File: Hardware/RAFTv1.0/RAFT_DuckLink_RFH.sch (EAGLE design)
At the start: 127 parts, among them J1 AMPHENOL_132134, J2 AMPHENOL_132134, J4 Micro-USB, J5 132134-15, Q1 SIA817EDJ, Q2 SI7288DP, Q3 2N7002, U1 SX1276, U10 PE4259, U2 MAX2771ETI+, U3 ESP32-D0WD, U4 W25Q16BVSSIG, U5 INTERFACE-CP2102-GMR(QFN28), U6 PE4259, U7 SP0503BAHT, U8 BQ24650RVAR, U9 TPS63070RNMT, Y1 32.768kHz

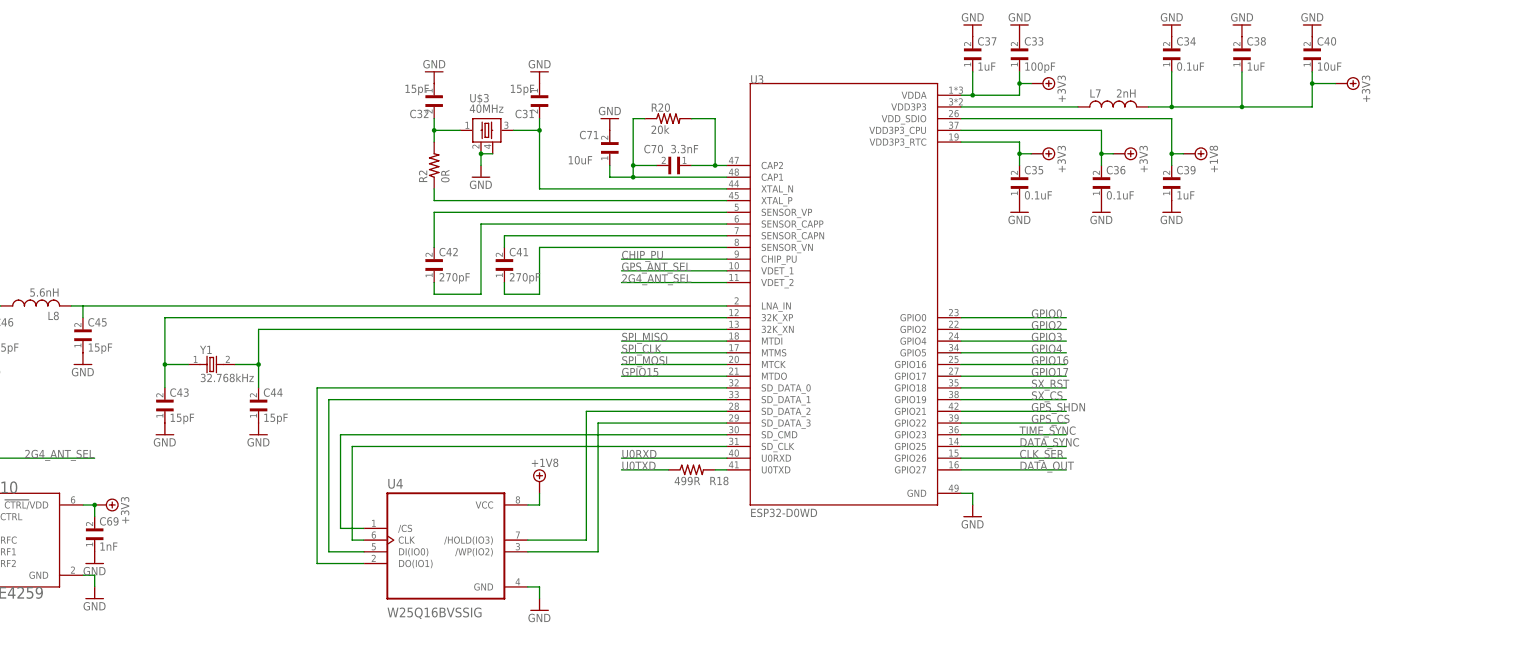
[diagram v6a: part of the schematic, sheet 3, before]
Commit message: fixed uart, updated pins
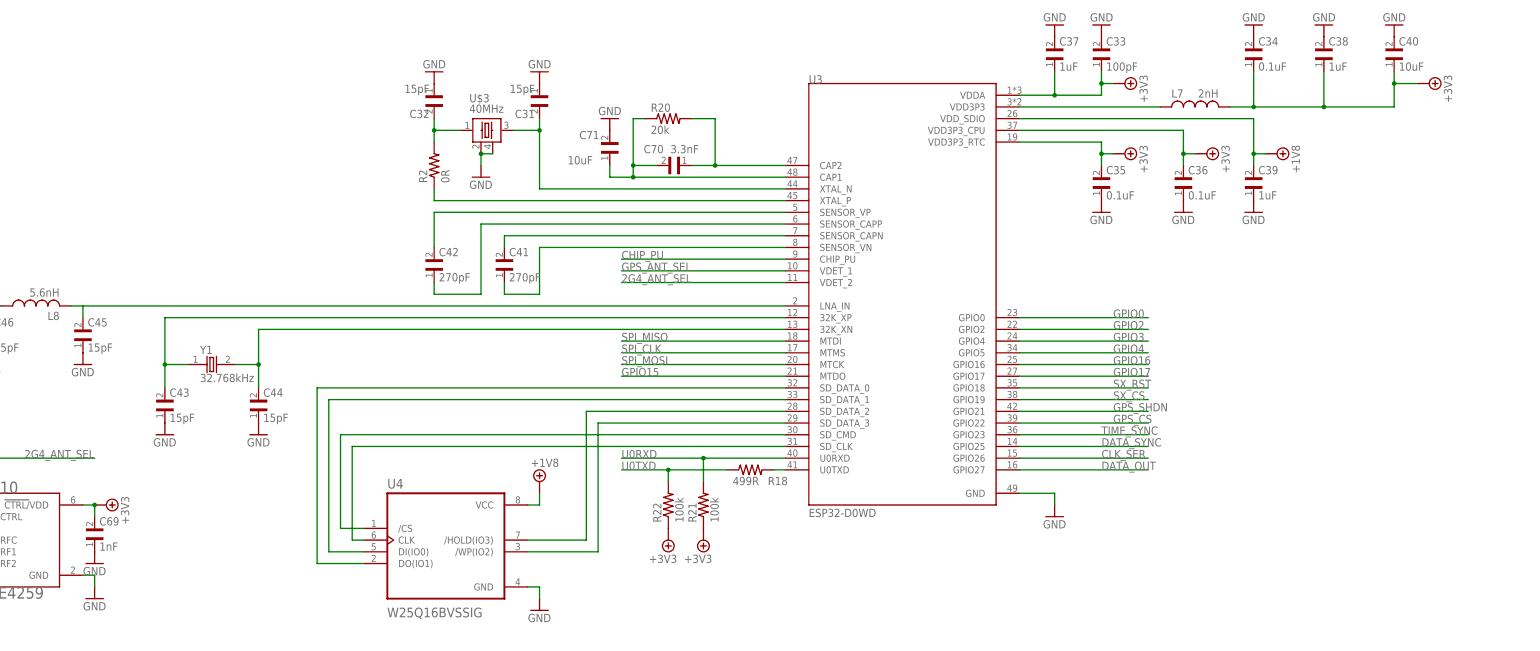
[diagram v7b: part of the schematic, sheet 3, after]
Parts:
- added R21, R22: 100k, RAFT-components:CRCW0402100KFKED
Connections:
- net +3.3V: now also R21.1, R22.1
- net U0RXD: now also R21.2
- net U0TXD: now also R22.2
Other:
- moved on the sheet: C33, C34, C35, C36, C37, C38, C39, C40, L7, R18, U3

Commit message: added libs for headers and switches (SparkFun). added sch page for io headers
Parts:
- added J3: (no value), SparkFun-Connectors:CONN_10X2
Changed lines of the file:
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@@
 <layer number="48" name="Document" color="7" fill="1" visible="no" active="no"/>
 <layer number="49" name="Reference" color="7" fill="1" visible="no" active="no"/>
+<layer number="50" name="dxf" color="7" fill="1" visible="no" active="no"/>
 <layer number="51" name="tDocu" color="7" fill="1" visible="no" active="no"/>
 <layer number="52" name="bDocu" color="7" fill="1" visible="no" active="no"/>
+<layer number="53" name="tGND_GNDA" color="7" fill="9" visible="no" active="no"/>
+<layer number="54" name="bGND_GNDA" color="1" fill="9" visible="no" active="no"/>
+<layer number="56" name="wert" color="7" fill="1" visible="no" active="no"/>
+<layer number="57" name="tCAD" color="7" fill="1" visible="no" active="no"/>
+<layer number="59" name="tCarbon" color="7" fill="1" visible="no" active="no"/>
+<layer number="60" name="bCarbon" color="7" fill="1" visible="no" active="no"/>
 <layer number="88" name="SimResults" color="9" fill="1" visible="yes" active="yes"/>
 <layer number="89" name="SimProbes" color="9" fill="1" visible="yes" active="yes"/>
@@
 <layer number="98" name="Guide" color="6" fill="1" visible="yes" active="yes"/>
 <layer number="99" name="SpiceOrder" color="7" fill="1" visible="yes" active="yes"/>
+<layer number="100" name="Muster" color="7" fill="1" visible="no" active="no"/>
+<layer number="101" name="Patch_Top" color="12" fill="4" visible="no" active="no"/>
+<layer number="102" name="Vscore" color="7" fill="1" visible="no" active="no"/>
+<layer number="103" name="tMap" color="7" fill="1" visible="no" active="no"/>
+<layer number="104" name="Name" color="16" fill="1" visible="no" active="no"/>
+<layer number="105" name="tPlate" color="7" fill="1" visible="no" active="no"/>
+<layer number="106" name="bPlate" color="7" fill="1" visible="no" active="no"/>
+<layer number="107" name="Crop" color="7" fill="1" visible="no" active="no"/>
+<layer number="108" name="tplace-old" color="10" fill="1" visible="no" active="no"/>
+<layer number="109" name="ref-old" color="11" fill="1" visible="no" active="no"/>
+<layer number="110" name="fp0" color="7" fill="1" visible="no" active="no"/>
+<layer number="111" name="LPC17xx" color="7" fill="1" visible="no" active="no"/>
+<layer number="112" name="tSilk" color="7" fill="1" visible="no" active="no"/>
+<layer number="113" name="IDFDebug" color="4" fill="1" visible="no" active="no"/>
+<layer number="114" name="Badge_Outline" color="7" fill="1" visible="no" active="no"/>
+<layer number="115" name="ReferenceISLANDS" color="7" fill="1" visible="no" active="no"/>
+<layer number="116" name="Patch_BOT" color="9" fill="4" visible="no" active="no"/>
+<layer number="117" name="PM_Ref" color="7" fill="1" visible="no" active="no"/>
+<layer number="118" name="Rect_Pads" color="7" fill="1" visible="no" active="no"/>
+<layer number="119" name="PF_Ref" color="7" fill="1" visible="no" active="no"/>
+<layer number="120" name="WFL_Ref" color="7" fill="1" visible="no" active="no"/>
+<layer number="121" name="_tsilk" color="7" fill="1" visible="no" active="no"/>
+<layer number="122" name="_bsilk" color="7" fill="1" visible="no" active="no"/>
+<layer number="123" name="tTestmark" color="7" fill="1" visible="no" active="no"/>
+<layer number="124" name="bTestmark" color="7" fill="1" visible="no" active="no"/>
+<layer number="125" name="_tNames" color="7" fill="1" visible="no" active="no"/>
+<layer number="126" name="_bNames" color="7" fill="1" visible="no" active="no"/>
+<layer number="127" name="_tValues" color="7" fill="1" visible="no" active="no"/>
+<layer number="128" name="_bValues" color="7" fill="1" visible="no" active="no"/>
+<layer number="129" name="Mask" color="7" fill="1" visible="no" active="no"/>
+<layer number="131" name="tAdjust" color="7" fill="1" visible="no" active="no"/>
+<layer number="132" name="bAdjust" color="7" fill="1" visible="no" active="no"/>
+<layer number="144" name="Drill_legend" color="7" fill="1" visible="no" active="no"/>
+<layer number="150" name="Notes" color="7" fill="1" visible="no" active="no"/>
+<layer number="151" name="HeatSink" color="7" fill="1" visible="no" active="no"/>
+<layer number="152" name="_bDocu" color="7" fill="1" visible="no" active="no"/>
+<layer number="153" name="FabDoc1" color="7" fill="1" visible="no" active="no"/>
+<layer number="154" name="FabDoc2" color="7" fill="1" visible="no" active="no"/>
+<layer number="155" name="FabDoc3" color="7" fill="1" visible="no" active="no"/>
+<layer number="199" name="Contour" color="7" fill="1" visible="no" active="no"/>
+<layer number="200" name="200bmp" color="1" fill="10" visible="no" active="no"/>
+<layer number="201" name="201bmp" color="2" fill="10" visible="no" active="no"/>
+<layer number="202" name="202bmp" color="3" fill="10" visible="no" active="no"/>
+<layer number="203" name="203bmp" color="4" fill="10" visible="no" active="no"/>
+<layer number="204" name="204bmp" color="5" fill="10" visible="no" active="no"/>
+<layer number="205" name="205bmp" color="6" fill="10" visible="no" active="no"/>
+<layer number="206" name="206bmp" color="7" fill="10" visible="no" active="no"/>
+<layer number="207" name="207bmp" color="8" fill="10" visible="no" active="no"/>
+<layer number="208" name="208bmp" color="9" fill="10" visible="no" active="no"/>
+<layer number="209" name="209bmp" color="7" fill="1" visible="no" active="no"/>
+<layer number="210" name="210bmp" color="7" fill="1" visible="no" active="no"/>
+<layer number="211" name="211bmp" color="7" fill="1" visible="no" active="no"/>
+<layer number="212" name="212bmp" color="7" fill="1" visible="no" active="no"/>
+<layer number="213" name="213bmp" color="7" fill="1" visible="no" active="no"/>
+<layer number="214" name="214bmp" color="7" fill="1" visible="no" active="no"/>
+<layer number="215" name="215bmp" color="7" fill="1" visible="no" active="no"/>
+<layer number="216" name="216bmp" color="7" fill="1" visible="no" active="no"/>
+<layer number="217" name="217bmp" color="18" fill="1" visible="no" active="no"/>
+<layer number="218" name="218bmp" color="19" fill="1" visible="no" active="no"/>
+<layer number="219" name="219bmp" color="20" fill="1" visible="no" active="no"/>
+<layer number="220" name="220bmp" color="21" fill="1" visible="no" active="no"/>
+<layer number="221" name="221bmp" color="22" fill="1" visible="no" active="no"/>
+<layer number="222" name="222bmp" color="23" fill="1" visible="no" active="no"/>
+<layer number="223" name="223bmp" color="24" fill="1" visible="no" active="no"/>
+<layer number="224" name="224bmp" color="25" fill="1" visible="no" active="no"/>
+<layer number="225" name="225bmp" color="7" fill="1" visible="no" active="no"/>
+<layer number="226" name="226bmp" color="7" fill="1" visible="no" active="no"/>
+<layer number="227" name="227bmp" color="7" fill="1" visible="no" active="no"/>
+<layer number="228" name="228bmp" color="7" fill="1" visible="no" active="no"/>
+<layer number="229" name="229bmp" color="7" fill="1" visible="no" active="no"/>
+<layer number="230" name="230bmp" color="7" fill="1" visible="no" active="no"/>
+<layer number="231" name="231bmp" color="7" fill="1" visible="no" active="no"/>
+<layer number="232" name="Eagle3D_PG2" color="7" fill="1" visible="no" active="no"/>
+<layer number="233" name="Eagle3D_PG3" color="7" fill="1" visible="no" active="no"/>
+<layer number="248" name="Housing" color="7" fill="1" visible="no" active="no"/>
+<layer number="249" name="Edge" color="7" fill="1" visible="no" active="no"/>
+<layer number="250" name="Descript" color="3" fill="1" visible="no" active="no"/>
+<layer number="251" name="SMDround" color="12" fill="11" visible="no" active="no"/>
+<layer number="254" name="cooling" color="7" fill="1" visible="no" active="no"/>
+<layer number="255" name="routoute" color="7" fill="1" visible="no" active="no"/>
 </layers>
 <schematic xreflabel="%F%N/%S.%C%R" xrefpart="/%S.%C%R">
@@
 <part name="SUPPLY19" library="supply3" deviceset="+3V3" device=""/>
 <part name="SUPPLY20" library="supply3" deviceset="+3V3" device=""/>
+<part name="J3" library="SparkFun-Connectors" deviceset="CONN_10X2" device=""/>
 </parts>
 <sheets>
@@
 </nets>
 </sheet>
+<sheet>
+<plain>
+</plain>
+<instances>
+<instance part="J3" gate="G$1" x="2.54" y="20.32" smashed="yes">
+<attribute name="VALUE" x="-1.27" y="2.794" size="1.778" layer="96" font="vector"/>
+<attribute name="NAME" x="-1.27" y="33.528" size="1.778" layer="95" font="vector"/>
+</instance>
+</instances>
+<busses>
+</busses>
+<nets>
+</nets>
+</sheet>
